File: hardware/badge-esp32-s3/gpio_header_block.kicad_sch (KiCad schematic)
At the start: 1 part

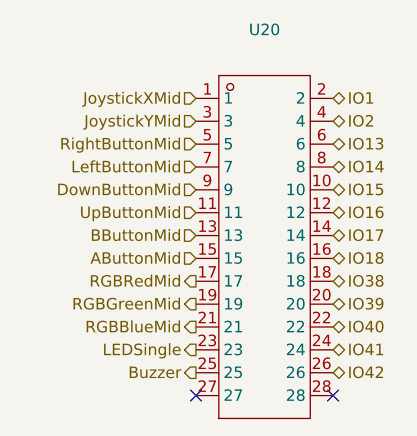
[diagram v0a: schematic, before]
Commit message: Consolidated the GPIO pins, communication pins, and power pins.
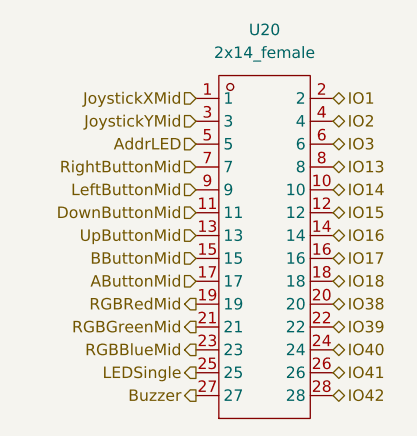
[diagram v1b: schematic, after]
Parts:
- U20: value ~ -> 2x14_female
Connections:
- net AButtonMid: now also U20.17; no longer U20.15
- net BButtonMid: now also U20.15; no longer U20.13
- net Buzzer: now also U20.27; no longer U20.25
- net DownButtonMid: now also U20.11; no longer U20.9
- net IO13: now also U20.8; no longer U20.6
- net IO14: now also U20.10; no longer U20.8
- net IO15: now also U20.12; no longer U20.10
- net IO16: now also U20.14; no longer U20.12
- net IO17: now also U20.16; no longer U20.14
- net IO18: now also U20.18; no longer U20.16
- net IO38: now also U20.20; no longer U20.18
- net IO39: now also U20.22; no longer U20.20
- net IO40: now also U20.24; no longer U20.22
- net IO41: now also U20.26; no longer U20.24
- net IO42: now also U20.28; no longer U20.26
- net LEDSingle: now also U20.25; no longer U20.23
- net LeftButtonMid: now also U20.9; no longer U20.7
- net RGBBlueMid: now also U20.23; no longer U20.21
- net RGBGreenMid: now also U20.21; no longer U20.19
- net RGBRedMid: now also U20.19; no longer U20.17
- net RightButtonMid: now also U20.7; no longer U20.5
- net UpButtonMid: now also U20.13; no longer U20.11
- new net AddrLED: U20.5
- new net IO3: U20.6
- no-connect marks 2 -> 0
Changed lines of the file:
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@@
 	(generator_version "9.0")
 	(paper "A4")
-	(no_connect
-		(at 137.16 107.95)
-	)
-	(no_connect
-		(at 121.92 107.95)
-	)
 	(hierarchical_label "IO1"
 		(shape bidirectional)
@@
 	(hierarchical_label "IO39"
 		(shape bidirectional)
+		(at 137.16 100.33 0)
+		(effects
+			(font
+				(size 1.27 1.27)
+			)
+			(justify left)
+		)
+	)
+	(hierarchical_label "IO38"
+		(shape bidirectional)
 		(at 137.16 97.79 0)
 		(effects
@@
 		)
 	)
-	(hierarchical_label "IO38"
+	(hierarchical_label "IO40"
+		(shape bidirectional)
+		(at 137.16 102.87 0)
+		(effects
+			(font
+				(size 1.27 1.27)
+			)
+			(justify left)
+		)
+	)
+	(hierarchical_label "IO41"
+		(shape bidirectional)
+		(at 137.16 105.41 0)
+		(effects
+			(font
+				(size 1.27 1.27)
+			)
+			(justify left)
+		)
+	)
+	(hierarchical_label "IO18"
 		(shape bidirectional)
 		(at 137.16 95.25 0)
@@
 		)
 	)
-	(hierarchical_label "IO40"
-		(shape bidirectional)
-		(at 137.16 100.33 0)
-		(effects
-			(font
-				(size 1.27 1.27)
-			)
-			(justify left)
-		)
-	)
-	(hierarchical_label "IO41"
-		(shape bidirectional)
-		(at 137.16 102.87 0)
-		(effects
-			(font
-				(size 1.27 1.27)
-			)
-			(justify left)
-		)
-	)
-	(hierarchical_label "IO18"
+	(hierarchical_label "IO14"
+		(shape bidirectional)
+		(at 137.16 85.09 0)
+		(effects
+			(font
+				(size 1.27 1.27)
+			)
+			(justify left)
+		)
+	)
+	(hierarchical_label "IO17"
 		(shape bidirectional)
 		(at 137.16 92.71 0)
@@
 		)
 	)
-	(hierarchical_label "IO14"
+	(hierarchical_label "IO15"
+		(shape bidirectional)
+		(at 137.16 87.63 0)
+		(effects
+			(font
+				(size 1.27 1.27)
+			)
+			(justify left)
+		)
+	)
+	(hierarchical_label "IO16"
+		(shape bidirectional)
+		(at 137.16 90.17 0)
+		(effects
+			(font
+				(size 1.27 1.27)
+			)
+			(justify left)
+		)
+	)
+	(hierarchical_label "IO13"
 		(shape bidirectional)
 		(at 137.16 82.55 0)
@@
 		)
 	)
-	(hierarchical_label "IO17"
-		(shape bidirectional)
-		(at 137.16 90.17 0)
-		(effects
-			(font
-				(size 1.27 1.27)
-			)
-			(justify left)
-		)
-	)
-	(hierarchical_label "IO15"
-		(shape bidirectional)
-		(at 137.16 85.09 0)
-		(effects
-			(font
-				(size 1.27 1.27)
-			)
-			(justify left)
-		)
-	)
-	(hierarchical_label "IO16"
-		(shape bidirectional)
-		(at 137.16 87.63 0)
-		(effects
-			(font
-				(size 1.27 1.27)
-			)
-			(justify left)
-		)
-	)
-	(hierarchical_label "IO13"
+	(hierarchical_label "IO42"
+		(shape bidirectional)
+		(at 137.16 107.95 0)
+		(effects
+			(font
+				(size 1.27 1.27)
+			)
+			(justify left)
+		)
+	)
+	(hierarchical_label "IO2"
+		(shape bidirectional)
+		(at 137.16 77.47 0)
+		(effects
+			(font
+				(size 1.27 1.27)
+			)
+			(justify left)
+		)
+	)
+	(hierarchical_label "DownButtonMid"
+		(shape input)
+		(at 121.92 87.63 180)
+		(effects
+			(font
+				(size 1.27 1.27)
+			)
+			(justify right)
+		)
+	)
+	(hierarchical_label "RightButtonMid"
+		(shape input)
+		(at 121.92 82.55 180)
+		(effects
+			(font
+				(size 1.27 1.27)
+			)
+			(justify right)
+		)
+	)
+	(hierarchical_label "LeftButtonMid"
+		(shape input)
+		(at 121.92 85.09 180)
+		(effects
+			(font
+				(size 1.27 1.27)
+			)
+			(justify right)
+		)
+	)
+	(hierarchical_label "UpButtonMid"
+		(shape input)
+		(at 121.92 90.17 180)
+		(effects
+			(font
+				(size 1.27 1.27)
+			)
+			(justify right)
+		)
+	)
+	(hierarchical_label "JoystickYMid"
+		(shape input)
+		(at 121.92 77.47 180)
+		(effects
+			(font
+				(size 1.27 1.27)
+			)
+			(justify right)
+		)
+	)
+	(hierarchical_label "RGBBlueMid"
+		(shape output)
+		(at 121.92 102.87 180)
+		(effects
+			(font
+				(size 1.27 1.27)
+			)
+			(justify right)
+		)
+	)
+	(hierarchical_label "LEDSingle"
+		(shape output)
+		(at 121.92 105.41 180)
+		(effects
+			(font
+				(size 1.27 1.27)
+			)
+			(justify right)
+		)
+	)
+	(hierarchical_label "RGBGreenMid"
+		(shape output)
+		(at 121.92 100.33 180)
+		(effects
+			(font
+				(size 1.27 1.27)
+			)
+			(justify right)
+		)
+	)
+	(hierarchical_label "Buzzer"
+		(shape output)
+		(at 121.92 107.95 180)
+		(effects
+			(font
+				(size 1.27 1.27)
+			)
+			(justify right)
+		)
+	)
+	(hierarchical_label "RGBRedMid"
+		(shape output)
+		(at 121.92 97.79 180)
+		(effects
+			(font
+				(size 1.27 1.27)
+			)
+			(justify right)
+		)
+	)
+	(hierarchical_label "BButtonMid"
+		(shape input)
+		(at 121.92 92.71 180)
+		(effects
+			(font
+				(size 1.27 1.27)
+			)
+			(justify right)
+		)
+	)
+	(hierarchical_label "AButtonMid"
+		(shape input)
+		(at 121.92 95.25 180)
+		(effects
+			(font
+				(size 1.27 1.27)
+			)
+			(justify right)
+		)
+	)
+	(hierarchical_label "AddrLED"
+		(shape input)
+		(at 121.92 80.01 180)
+		(effects
+			(font
+				(size 1.27 1.27)
+			)
+			(justify right)
+		)
+	)
+	(hierarchical_label "IO3"
 		(shape bidirectional)
 		(at 137.16 80.01 0)
@@
 			)
 			(justify left)
-		)
-	)
-	(hierarchical_label "IO42"
-		(shape bidirectional)
-		(at 137.16 105.41 0)
-		(effects
-			(font
-				(size 1.27 1.27)
-			)
-			(justify left)
-		)
-	)
-	(hierarchical_label "IO2"
-		(shape bidirectional)
-		(at 137.16 77.47 0)
-		(effects
-			(font
-				(size 1.27 1.27)
-			)
-			(justify left)
-		)
-	)
-	(hierarchical_label "DownButtonMid"
-		(shape input)
-		(at 121.92 85.09 180)
-		(effects
-			(font
-				(size 1.27 1.27)
-			)
-			(justify right)
-		)
-	)
-	(hierarchical_label "RightButtonMid"
-		(shape input)
-		(at 121.92 80.01 180)
-		(effects
-			(font
-				(size 1.27 1.27)
-			)
-			(justify right)
-		)
-	)
-	(hierarchical_label "LeftButtonMid"
-		(shape input)
-		(at 121.92 82.55 180)
-		(effects
-			(font
-				(size 1.27 1.27)
-			)
-			(justify right)
-		)
-	)
-	(hierarchical_label "UpButtonMid"
-		(shape input)
-		(at 121.92 87.63 180)
-		(effects
-			(font
-				(size 1.27 1.27)
-			)
-			(justify right)
-		)
-	)
-	(hierarchical_label "JoystickYMid"
-		(shape input)
-		(at 121.92 77.47 180)
-		(effects
-			(font
-				(size 1.27 1.27)
-			)
-			(justify right)
-		)
-	)
-	(hierarchical_label "RGBBlueMid"
-		(shape output)
-		(at 121.92 100.33 180)
-		(effects
-			(font
-				(size 1.27 1.27)
-			)
-			(justify right)
-		)
-	)
-	(hierarchical_label "LEDSingle"
-		(shape output)
-		(at 121.92 102.87 180)
-		(effects
-			(font
-				(size 1.27 1.27)
-			)
-			(justify right)
-		)
-	)
-	(hierarchical_label "RGBGreenMid"
-		(shape output)
-		(at 121.92 97.79 180)
-		(effects
-			(font
-				(size 1.27 1.27)
-			)
-			(justify right)
-		)
-	)
-	(hierarchical_label "Buzzer"
-		(shape output)
-		(at 121.92 105.41 180)
-		(effects
-			(font
-				(size 1.27 1.27)
-			)
-			(justify right)
-		)
-	)
-	(hierarchical_label "RGBRedMid"
-		(shape output)
-		(at 121.92 95.25 180)
-		(effects
-			(font
-				(size 1.27 1.27)
-			)
-			(justify right)
-		)
-	)
-	(hierarchical_label "BButtonMid"
-		(shape input)
-		(at 121.92 90.17 180)
-		(effects
-			(font
-				(size 1.27 1.27)
-			)
-			(justify right)
-		)
-	)
-	(hierarchical_label "AButtonMid"
-		(shape input)
-		(at 121.92 92.71 180)
-		(effects
-			(font
-				(size 1.27 1.27)
-			)
-			(justify right)
 		)
 	)
@@
 			)
 		)
-		(property "Value" "~"
+		(property "Value" "2x14_female"
 			(at 129.54 69.85 0)
 			(effects

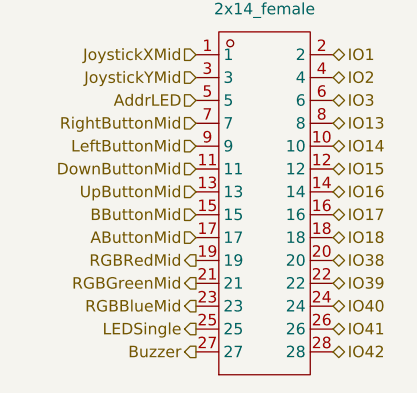
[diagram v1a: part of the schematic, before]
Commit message: Swapped the RGB led pins.
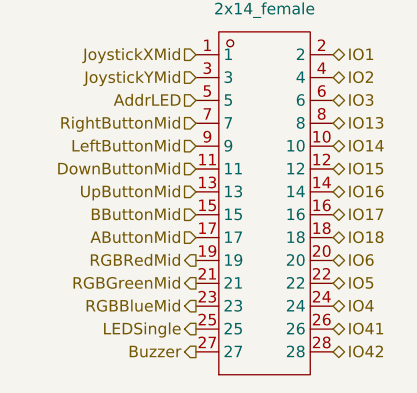
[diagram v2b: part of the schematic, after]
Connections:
- net IO38 renamed IO6
- net IO39 renamed IO5
- net IO40 renamed IO4
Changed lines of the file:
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@@
 		)
 	)
-	(hierarchical_label "IO39"
+	(hierarchical_label "IO5"
 		(shape bidirectional)
 		(at 137.16 100.33 0)
@@
 		)
 	)
-	(hierarchical_label "IO38"
+	(hierarchical_label "IO6"
 		(shape bidirectional)
 		(at 137.16 97.79 0)
@@
 		)
 	)
-	(hierarchical_label "IO40"
+	(hierarchical_label "IO4"
 		(shape bidirectional)
 		(at 137.16 102.87 0)

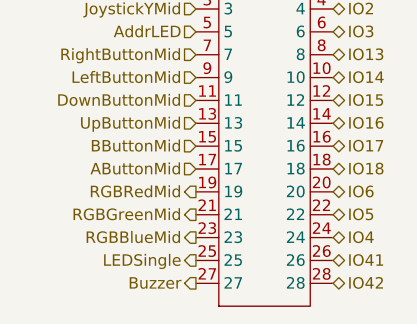
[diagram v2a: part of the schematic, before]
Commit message: Updated the buzzer to not use a jtag pin.
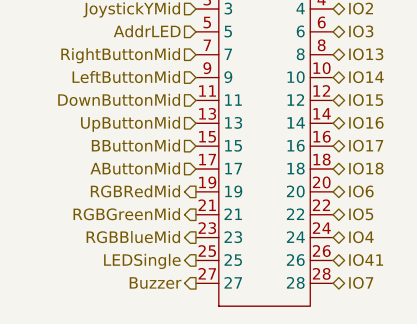
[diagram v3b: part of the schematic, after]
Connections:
- net IO42 renamed IO7
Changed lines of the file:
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@@
 		)
 	)
-	(hierarchical_label "IO42"
+	(hierarchical_label "IO7"
 		(shape bidirectional)
 		(at 137.16 107.95 0)

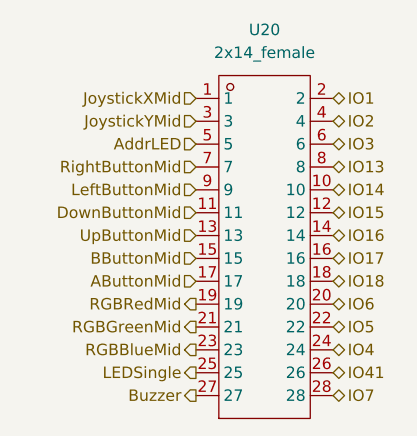
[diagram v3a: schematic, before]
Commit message: Updated pins
Updated pins and headers to avoid using internal flash SPI pins on schematic.
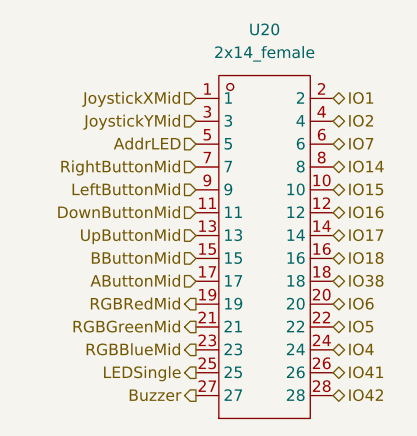
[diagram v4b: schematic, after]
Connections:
- net IO13 is gone; now on net IO14: U20.8
- net IO3 is gone; now on net IO7: U20.6
- net IO14: no longer U20.10
- net IO15: now also U20.10; no longer U20.12
- net IO16: now also U20.12; no longer U20.14
- net IO17: now also U20.14; no longer U20.16
- net IO18: now also U20.16; no longer U20.18
- net IO7: no longer U20.28
- new net IO38: U20.18
- new net IO42: U20.28
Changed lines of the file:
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@@
+		)
+	)
+	(hierarchical_label "IO38"
+		(shape bidirectional)
+		(at 137.16 95.25 0)
+		(effects
+			(font
+				(size 1.27 1.27)
+			)
+			(justify left)
+		)
+	)
+	(hierarchical_label "IO15"
+		(shape bidirectional)
+		(at 137.16 85.09 0)
+		(effects
+			(font
+				(size 1.27 1.27)
+			)
+			(justify left)
 		)
 	)
 	(hierarchical_label "IO18"
 		(shape bidirectional)
-		(at 137.16 95.25 0)
+		(at 137.16 92.71 0)
+		(effects
+			(font
+				(size 1.27 1.27)
+			)
+			(justify left)
+		)
+	)
+	(hierarchical_label "IO16"
+		(shape bidirectional)
+		(at 137.16 87.63 0)
+		(effects
+			(font
+				(size 1.27 1.27)
+			)
+			(justify left)
+		)
+	)
+	(hierarchical_label "IO17"
+		(shape bidirectional)
+		(at 137.16 90.17 0)
 		(effects
 			(font
@@
 	(hierarchical_label "IO14"
 		(shape bidirectional)
-		(at 137.16 85.09 0)
-		(effects
-			(font
-				(size 1.27 1.27)
-			)
-			(justify left)
-		)
-	)
-	(hierarchical_label "IO17"
-		(shape bidirectional)
-		(at 137.16 92.71 0)
-		(effects
-			(font
-				(size 1.27 1.27)
-			)
-			(justify left)
-		)
-	)
-	(hierarchical_label "IO15"
-		(shape bidirectional)
-		(at 137.16 87.63 0)
-		(effects
-			(font
-				(size 1.27 1.27)
-			)
-			(justify left)
-		)
-	)
-	(hierarchical_label "IO16"
-		(shape bidirectional)
-		(at 137.16 90.17 0)
-		(effects
-			(font
-				(size 1.27 1.27)
-			)
-			(justify left)
-		)
-	)
-	(hierarchical_label "IO13"
-		(shape bidirectional)
 		(at 137.16 82.55 0)
 		(effects
@@
 		)
 	)
+	(hierarchical_label "IO42"
+		(shape bidirectional)
+		(at 137.16 107.95 0)
+		(effects
+			(font
+				(size 1.27 1.27)
+			)
+			(justify left)
+		)
+	)
+	(hierarchical_label "IO2"
+		(shape bidirectional)
+		(at 137.16 77.47 0)
+		(effects
+			(font
+				(size 1.27 1.27)
+			)
+			(justify left)
+		)
+	)
+	(hierarchical_label "DownButtonMid"
+		(shape input)
+		(at 121.92 87.63 180)
+		(effects
+			(font
+				(size 1.27 1.27)
+			)
+			(justify right)
+		)
+	)
+	(hierarchical_label "RightButtonMid"
+		(shape input)
+		(at 121.92 82.55 180)
+		(effects
+			(font
+				(size 1.27 1.27)
+			)
+			(justify right)
+		)
+	)
+	(hierarchical_label "LeftButtonMid"
+		(shape input)
+		(at 121.92 85.09 180)
+		(effects
+			(font
+				(size 1.27 1.27)
+			)
+			(justify right)
+		)
+	)
+	(hierarchical_label "UpButtonMid"
+		(shape input)
+		(at 121.92 90.17 180)
+		(effects
+			(font
+				(size 1.27 1.27)
+			)
+			(justify right)
+		)
+	)
+	(hierarchical_label "JoystickYMid"
+		(shape input)
+		(at 121.92 77.47 180)
+		(effects
+			(font
+				(size 1.27 1.27)
+			)
+			(justify right)
+		)
+	)
+	(hierarchical_label "RGBBlueMid"
+		(shape output)
+		(at 121.92 102.87 180)
+		(effects
+			(font
+				(size 1.27 1.27)
+			)
+			(justify right)
+		)
+	)
+	(hierarchical_label "LEDSingle"
+		(shape output)
+		(at 121.92 105.41 180)
+		(effects
+			(font
+				(size 1.27 1.27)
+			)
+			(justify right)
+		)
+	)
+	(hierarchical_label "RGBGreenMid"
+		(shape output)
+		(at 121.92 100.33 180)
+		(effects
+			(font
+				(size 1.27 1.27)
+			)
+			(justify right)
+		)
+	)
+	(hierarchical_label "Buzzer"
+		(shape output)
+		(at 121.92 107.95 180)
+		(effects
+			(font
+				(size 1.27 1.27)
+			)
+			(justify right)
+		)
+	)
+	(hierarchical_label "RGBRedMid"
+		(shape output)
+		(at 121.92 97.79 180)
+		(effects
+			(font
+				(size 1.27 1.27)
+			)
+			(justify right)
+		)
+	)
+	(hierarchical_label "BButtonMid"
+		(shape input)
+		(at 121.92 92.71 180)
+		(effects
+			(font
+				(size 1.27 1.27)
+			)
+			(justify right)
+		)
+	)
+	(hierarchical_label "AButtonMid"
+		(shape input)
+		(at 121.92 95.25 180)
+		(effects
+			(font
+				(size 1.27 1.27)
+			)
+			(justify right)
+		)
+	)
+	(hierarchical_label "AddrLED"
+		(shape input)
+		(at 121.92 80.01 180)
+		(effects
+			(font
+				(size 1.27 1.27)
+			)
+			(justify right)
+		)
+	)
 	(hierarchical_label "IO7"
 		(shape bidirectional)
-		(at 137.16 107.95 0)
-		(effects
-			(font
-				(size 1.27 1.27)
-			)
-			(justify left)
-		)
-	)
-	(hierarchical_label "IO2"
-		(shape bidirectional)
-		(at 137.16 77.47 0)
-		(effects
-			(font
-				(size 1.27 1.27)
-			)
-			(justify left)
-		)
-	)
-	(hierarchical_label "DownButtonMid"
-		(shape input)
-		(at 121.92 87.63 180)
-		(effects
-			(font
-				(size 1.27 1.27)
-			)
-			(justify right)
-		)
-	)
-	(hierarchical_label "RightButtonMid"
-		(shape input)
-		(at 121.92 82.55 180)
-		(effects
-			(font
-				(size 1.27 1.27)
-			)
-			(justify right)
-		)
-	)
-	(hierarchical_label "LeftButtonMid"
-		(shape input)
-		(at 121.92 85.09 180)
-		(effects
-			(font
-				(size 1.27 1.27)
-			)
-			(justify right)
-		)
-	)
-	(hierarchical_label "UpButtonMid"
-		(shape input)
-		(at 121.92 90.17 180)
-		(effects
-			(font
-				(size 1.27 1.27)
-			)
-			(justify right)
-		)
-	)
-	(hierarchical_label "JoystickYMid"
-		(shape input)
-		(at 121.92 77.47 180)
-		(effects
-			(font
-				(size 1.27 1.27)
-			)
-			(justify right)
-		)
-	)
-	(hierarchical_label "RGBBlueMid"
-		(shape output)
-		(at 121.92 102.87 180)
-		(effects
-			(font
-				(size 1.27 1.27)
-			)
-			(justify right)
-		)
-	)
-	(hierarchical_label "LEDSingle"
-		(shape output)
-		(at 121.92 105.41 180)
-		(effects
-			(font
-				(size 1.27 1.27)
-			)
-			(justify right)
-		)
-	)
-	(hierarchical_label "RGBGreenMid"
-		(shape output)
-		(at 121.92 100.33 180)
-		(effects
-			(font
-				(size 1.27 1.27)
-			)
-			(justify right)
-		)
-	)
-	(hierarchical_label "Buzzer"
-		(shape output)
-		(at 121.92 107.95 180)
-		(effects
-			(font
-				(size 1.27 1.27)
-			)
-			(justify right)
-		)
-	)
-	(hierarchical_label "RGBRedMid"
-		(shape output)
-		(at 121.92 97.79 180)
-		(effects
-			(font
-				(size 1.27 1.27)
-			)
-			(justify right)
-		)
-	)
-	(hierarchical_label "BButtonMid"
-		(shape input)
-		(at 121.92 92.71 180)
-		(effects
-			(font
-				(size 1.27 1.27)
-			)
-			(justify right)
-		)
-	)
-	(hierarchical_label "AButtonMid"
-		(shape input)
-		(at 121.92 95.25 180)
-		(effects
-			(font
-				(size 1.27 1.27)
-			)
-			(justify right)
-		)
-	)
-	(hierarchical_label "AddrLED"
-		(shape input)
-		(at 121.92 80.01 180)
-		(effects
-			(font
-				(size 1.27 1.27)
-			)
-			(justify right)
-		)
-	)
-	(hierarchical_label "IO3"
-		(shape bidirectional)
 		(at 137.16 80.01 0)
